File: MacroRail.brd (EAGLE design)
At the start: 42.9 x 81.5 mm, 20 parts, among them CN1 1X4-3.5MM, J1 SJ1-2503A, U1 ESP32DEVKITC, U2 TCM2209-V1.2

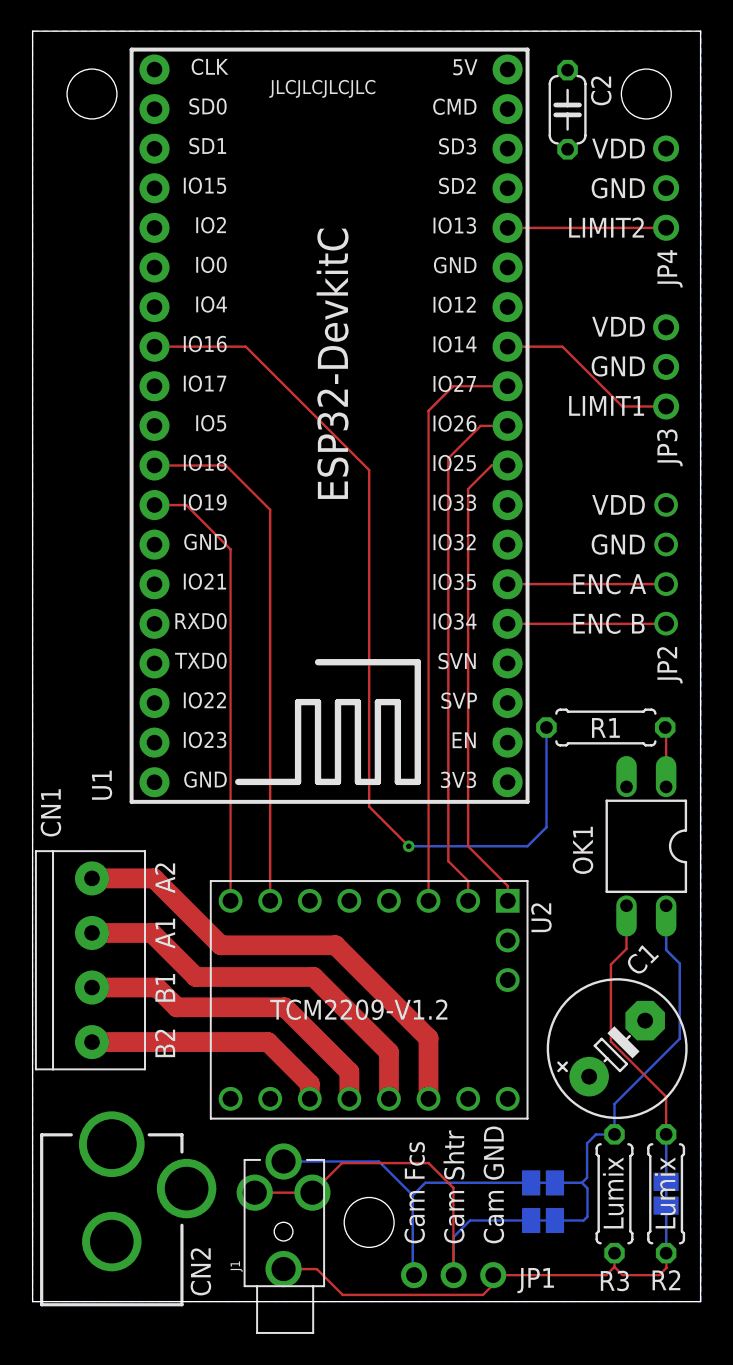
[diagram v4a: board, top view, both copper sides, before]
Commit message: Start V1.1 design
Add UART Communication between TCM and ESP via SD2 and SD3 pins. Connect DIAG pin. Still undecided whether INDEX pin is necessary as this pin is not always easily accessible on TCM boards.
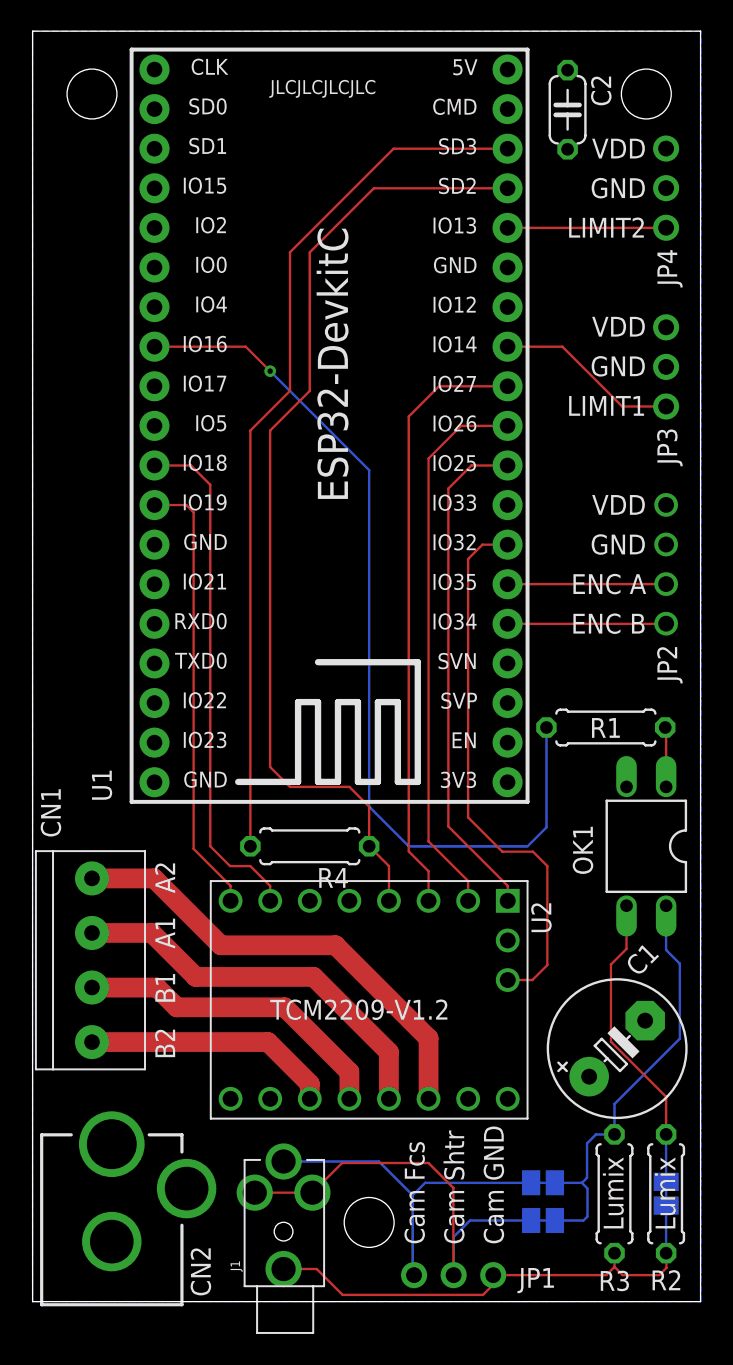
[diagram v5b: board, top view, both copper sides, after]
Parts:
- added R4: 1k, rcl:0207/7
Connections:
- removed net STEP_PDN_1: U2.PDN_1
- removed net STEP_UART_CLK: U2.CLK
- new net N$2: U1.8
- new net STEP_DIAG: U1.7, U2.DIAG
- new net U1RXD: R4.1, U1.16, U2.PDN_1
- new net U1TXD: R4.2, U1.17
- net GND: now also U2.CLK
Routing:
- net U1RXD: track 0.00 -> 62.4 mm
- net U1TXD: track 0.00 -> 55.9 mm
- net STEP_DIAG: track 0.00 -> 35.2 mm
- net STEP_EN: track 30.6 -> 32.4 mm
- net STEP_MS1: track 33.6 -> 35.4 mm
- net STEP_MS2: track 37.2 -> 38.7 mm
- net STEP: track 33.7 -> 33.1 mm
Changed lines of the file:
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@@
 <attribute name="VALUE" x="31.526" y="78.746" size="1.27" layer="27" ratio="10" rot="R270"/>
+</element>
+<element name="R4" library="rcl" library_urn="urn:adsk.eagle:library:334" package="0207/7" package3d_urn="urn:adsk.eagle:package:23493/2" value="1k" x="17.78" y="29.21" smashed="yes" rot="R180">
+<attribute name="NAME" x="20.32" y="27.813" size="1.27" layer="25" ratio="10" rot="R180"/>
+<attribute name="POPULARITY" value="22" x="17.78" y="29.21" size="1.778" layer="27" rot="R180" display="off"/>
+<attribute name="SPICEPREFIX" value="R" x="17.78" y="29.21" size="1.778" layer="27" rot="R180" display="off"/>
+<attribute name="VALUE" x="20.066" y="29.7688" size="1.27" layer="27" ratio="10" rot="R180"/>
 </element>
 </elements>
@@
 <contactref element="OK1" pad="2"/>
 <contactref element="C2" pad="1"/>
+<contactref element="U2" pad="CLK"/>
 </signal>
 <signal name="A2" class="1">
@@
 <contactref element="U2" pad="EN"/>
 <contactref element="U1" pad="9"/>
-<wire x1="30.47" y1="53.64" x2="29.454" y2="53.64" width="0.1524" layer="1"/>
-<wire x1="29.454" y1="53.64" x2="27.94" y2="52.126" width="0.1524" layer="1"/>
-<wire x1="27.94" y1="29.21" x2="30.48" y2="26.67" width="0.1524" layer="1"/>
+<wire x1="30.47" y1="53.64" x2="28.154" y2="53.64" width="0.1524" layer="1"/>
+<wire x1="28.154" y1="53.64" x2="26.67" y2="52.156" width="0.1524" layer="1"/>
+<wire x1="26.67" y1="30.48" x2="30.48" y2="26.67" width="0.1524" layer="1"/>
 <wire x1="30.48" y1="26.67" x2="30.48" y2="25.71" width="0.1524" layer="1"/>
-<wire x1="27.94" y1="52.126" x2="27.94" y2="29.21" width="0.1524" layer="1"/>
+<wire x1="26.67" y1="52.156" x2="26.67" y2="30.48" width="0.1524" layer="1"/>
 </signal>
 <signal name="STEP_MS1">
 <contactref element="U2" pad="MS1"/>
 <contactref element="U1" pad="10"/>
-<wire x1="26.67" y1="54.102" x2="26.67" y2="28.25" width="0.1524" layer="1"/>
+<wire x1="25.4" y1="54.092" x2="25.4" y2="29.52" width="0.1524" layer="1"/>
 <wire x1="27.94" y1="25.71" x2="27.94" y2="26.98" width="0.1524" layer="1"/>
-<wire x1="27.94" y1="26.98" x2="26.67" y2="28.25" width="0.1524" layer="1"/>
-<wire x1="28.748" y1="56.18" x2="30.47" y2="56.18" width="0.1524" layer="1"/>
-<wire x1="26.67" y1="54.102" x2="28.748" y2="56.18" width="0.1524" layer="1"/>
+<wire x1="27.94" y1="26.98" x2="25.4" y2="29.52" width="0.1524" layer="1"/>
+<wire x1="27.488" y1="56.18" x2="30.47" y2="56.18" width="0.1524" layer="1"/>
+<wire x1="25.4" y1="54.092" x2="27.488" y2="56.18" width="0.1524" layer="1"/>
 </signal>
 <signal name="STEP_MS2">
 <contactref element="U2" pad="MS2"/>
 <contactref element="U1" pad="11"/>
-<wire x1="25.4" y1="25.71" x2="25.4" y2="57.15" width="0.1524" layer="1"/>
-<wire x1="26.97" y1="58.72" x2="30.47" y2="58.72" width="0.1524" layer="1"/>
-<wire x1="25.4" y1="57.15" x2="26.97" y2="58.72" width="0.1524" layer="1"/>
-</signal>
-<signal name="STEP_PDN_1">
-<contactref element="U2" pad="PDN_1"/>
+<wire x1="24.13" y1="56.78" x2="24.13" y2="28.88" width="0.1524" layer="1"/>
+<wire x1="25.4" y1="25.71" x2="25.4" y2="27.61" width="0.1524" layer="1"/>
+<wire x1="25.4" y1="27.61" x2="24.13" y2="28.88" width="0.1524" layer="1"/>
+<wire x1="26.07" y1="58.72" x2="30.47" y2="58.72" width="0.1524" layer="1"/>
+<wire x1="24.13" y1="56.78" x2="26.07" y2="58.72" width="0.1524" layer="1"/>
 </signal>
 <signal name="STEP_PDN_2">
 <contactref element="U2" pad="PDN_2"/>
-</signal>
-<signal name="STEP_UART_CLK">
-<contactref element="U2" pad="CLK"/>
 </signal>
 <signal name="STEP">
 <contactref element="U2" pad="STEP"/>
 <contactref element="U1" pad="30"/>
-<wire x1="15.24" y1="25.71" x2="15.24" y2="50.8" width="0.1524" layer="1"/>
-<wire x1="12.4" y1="53.64" x2="7.82" y2="53.64" width="0.1524" layer="1"/>
-<wire x1="15.24" y1="50.8" x2="12.4" y2="53.64" width="0.1524" layer="1"/>
+<wire x1="15.24" y1="25.71" x2="15.24" y2="26.67" width="0.1524" layer="1"/>
+<wire x1="15.24" y1="26.67" x2="13.97" y2="27.94" width="0.1524" layer="1"/>
+<wire x1="7.82" y1="53.64" x2="10.16" y2="53.64" width="0.1524" layer="1"/>
+<wire x1="10.16" y1="53.64" x2="11.4" y2="52.4" width="0.1524" layer="1"/>
+<wire x1="11.4" y1="29.21" x2="11.4" y2="52.4" width="0.1524" layer="1"/>
+<wire x1="12.67" y1="27.94" x2="11.4" y2="29.21" width="0.1524" layer="1"/>
+<wire x1="13.97" y1="27.94" x2="12.67" y2="27.94" width="0.1524" layer="1"/>
 </signal>
 <signal name="STEP_DIR">
@@
 <contactref element="U1" pad="31"/>
 <wire x1="9.86" y1="51.1" x2="7.82" y2="51.1" width="0.1524" layer="1"/>
-<wire x1="12.7" y1="25.71" x2="12.7" y2="48.26" width="0.1524" layer="1"/>
-<wire x1="12.7" y1="48.26" x2="9.86" y2="51.1" width="0.1524" layer="1"/>
+<wire x1="12.7" y1="25.71" x2="12.7" y2="26.67" width="0.1524" layer="1"/>
+<wire x1="10.33" y1="50.63" x2="9.86" y2="51.1" width="0.1524" layer="1"/>
+<wire x1="12.7" y1="26.67" x2="10.33" y2="29.04" width="0.1524" layer="1"/>
+<wire x1="10.33" y1="29.04" x2="10.33" y2="50.63" width="0.1524" layer="1"/>
 </signal>
 <signal name="SHUTTER">
@@
 <contactref element="R1" pad="2"/>
 <wire x1="7.82" y1="61.26" x2="13.67" y2="61.26" width="0.1524" layer="1"/>
-<wire x1="21.59" y1="31.75" x2="24.13" y2="29.21" width="0.1524" layer="1"/>
-<via x="24.13" y="29.21" extent="1-16" drill="0.35"/>
-<wire x1="13.67" y1="61.26" x2="21.59" y2="53.34" width="0.1524" layer="1"/>
-<wire x1="21.59" y1="53.34" x2="21.59" y2="31.75" width="0.1524" layer="1"/>
+<wire x1="13.67" y1="61.26" x2="15.24" y2="59.69" width="0.1524" layer="1"/>
 <wire x1="24.13" y1="29.21" x2="31.75" y2="29.21" width="0.1524" layer="16"/>
 <wire x1="32.964" y1="36.83" x2="32.964" y2="30.424" width="0.1524" layer="16"/>
 <wire x1="32.964" y1="30.424" x2="31.75" y2="29.21" width="0.1524" layer="16"/>
+<wire x1="24.13" y1="29.21" x2="21.59" y2="31.75" width="0.1524" layer="16"/>
+<wire x1="21.59" y1="53.34" x2="15.24" y2="59.69" width="0.1524" layer="16"/>
+<via x="15.24" y="59.69" extent="1-16" drill="0.35"/>
+<wire x1="21.59" y1="31.75" x2="21.59" y2="53.34" width="0.1524" layer="16"/>
 </signal>
 <signal name="LIMIT1">
@@
 <wire x1="40.64" y1="36.774" x2="40.64" y2="33.02" width="0.1524" layer="1"/>
 </signal>
+<signal name="U1TXD">
+<contactref element="R4" pad="2"/>
+<contactref element="U1" pad="17"/>
+<wire x1="30.47" y1="73.96" x2="23.16" y2="73.96" width="0.1524" layer="1"/>
+<wire x1="16.51" y1="67.31" x2="16.51" y2="58.42" width="0.1524" layer="1"/>
+<wire x1="16.51" y1="58.42" x2="13.97" y2="55.88" width="0.1524" layer="1"/>
+<wire x1="13.97" y1="55.88" x2="13.97" y2="29.21" width="0.1524" layer="1"/>
+<wire x1="23.16" y1="73.96" x2="16.51" y2="67.31" width="0.1524" layer="1"/>
+</signal>
+<signal name="U1RXD">
+<contactref element="R4" pad="1"/>
+<contactref element="U2" pad="PDN_1"/>
+<contactref element="U1" pad="16"/>
+<wire x1="21.59" y1="29.21" x2="21.59" y2="31.75" width="0.1524" layer="1"/>
+<wire x1="21.59" y1="31.75" x2="20.32" y2="33.02" width="0.1524" layer="1"/>
+<wire x1="20.32" y1="33.02" x2="16.51" y2="33.02" width="0.1524" layer="1"/>
+<wire x1="16.51" y1="33.02" x2="15.24" y2="34.29" width="0.1524" layer="1"/>
+<wire x1="15.24" y1="55.88" x2="17.78" y2="58.42" width="0.1524" layer="1"/>
+<wire x1="17.78" y1="58.42" x2="17.78" y2="67.31" width="0.1524" layer="1"/>
+<wire x1="17.78" y1="67.31" x2="21.89" y2="71.42" width="0.1524" layer="1"/>
+<wire x1="21.89" y1="71.42" x2="30.47" y2="71.42" width="0.1524" layer="1"/>
+<wire x1="15.24" y1="34.29" x2="15.24" y2="55.88" width="0.1524" layer="1"/>
+<wire x1="22.86" y1="25.71" x2="22.86" y2="27.94" width="0.1524" layer="1"/>
+<wire x1="22.86" y1="27.94" x2="21.59" y2="29.21" width="0.1524" layer="1"/>
+</signal>
+<signal name="STEP_DIAG">
+<contactref element="U2" pad="DIAG"/>
+<contactref element="U1" pad="7"/>
+<wire x1="30.47" y1="48.56" x2="28.86" y2="48.56" width="0.1524" layer="1"/>
+<wire x1="28.86" y1="48.56" x2="27.94" y2="47.64" width="0.1524" layer="1"/>
+<wire x1="27.94" y1="47.64" x2="27.94" y2="31.06" width="0.1524" layer="1"/>
+<wire x1="33.02" y1="21.59" x2="32.06" y2="20.63" width="0.1524" layer="1"/>
+<wire x1="32.06" y1="20.63" x2="30.48" y2="20.63" width="0.1524" layer="1"/>
+<wire x1="27.94" y1="31.06" x2="30.135" y2="28.865" width="0.1524" layer="1"/>
+<wire x1="30.135" y1="28.865" x2="32.095" y2="28.865" width="0.1524" layer="1"/>
+<wire x1="32.095" y1="28.865" x2="33.02" y2="27.94" width="0.1524" layer="1"/>
+<wire x1="33.02" y1="27.94" x2="33.02" y2="21.59" width="0.1524" layer="1"/>
+</signal>
+<signal name="N$2">
+<contactref element="U1" pad="8"/>
+</signal>
 </signals>

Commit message: Connect DIAG
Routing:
- net U1TXD: track 55.9 -> 58.1 mm
- net U1RXD: track 62.4 -> 63.2 mm
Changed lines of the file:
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@@
 <contactref element="R4" pad="2"/>
 <contactref element="U1" pad="17"/>
-<wire x1="30.47" y1="73.96" x2="23.16" y2="73.96" width="0.1524" layer="1"/>
-<wire x1="16.51" y1="67.31" x2="16.51" y2="58.42" width="0.1524" layer="1"/>
+<wire x1="30.47" y1="73.96" x2="19.35" y2="73.96" width="0.1524" layer="1"/>
+<wire x1="16.51" y1="71.12" x2="16.51" y2="58.42" width="0.1524" layer="1"/>
 <wire x1="16.51" y1="58.42" x2="13.97" y2="55.88" width="0.1524" layer="1"/>
 <wire x1="13.97" y1="55.88" x2="13.97" y2="29.21" width="0.1524" layer="1"/>
-<wire x1="23.16" y1="73.96" x2="16.51" y2="67.31" width="0.1524" layer="1"/>
+<wire x1="19.35" y1="73.96" x2="16.51" y2="71.12" width="0.1524" layer="1"/>
 </signal>
 <signal name="U1RXD">
@@
 <wire x1="20.32" y1="33.02" x2="16.51" y2="33.02" width="0.1524" layer="1"/>
 <wire x1="16.51" y1="33.02" x2="15.24" y2="34.29" width="0.1524" layer="1"/>
-<wire x1="15.24" y1="55.88" x2="17.78" y2="58.42" width="0.1524" layer="1"/>
-<wire x1="17.78" y1="58.42" x2="17.78" y2="67.31" width="0.1524" layer="1"/>
-<wire x1="17.78" y1="67.31" x2="21.89" y2="71.42" width="0.1524" layer="1"/>
-<wire x1="21.89" y1="71.42" x2="30.47" y2="71.42" width="0.1524" layer="1"/>
-<wire x1="15.24" y1="34.29" x2="15.24" y2="55.88" width="0.1524" layer="1"/>
+<wire x1="15.24" y1="54.61" x2="17.78" y2="57.15" width="0.1524" layer="1"/>
+<wire x1="17.78" y1="57.15" x2="17.78" y2="68.58" width="0.1524" layer="1"/>
+<wire x1="17.78" y1="68.58" x2="20.62" y2="71.42" width="0.1524" layer="1"/>
+<wire x1="20.62" y1="71.42" x2="30.47" y2="71.42" width="0.1524" layer="1"/>
+<wire x1="15.24" y1="34.29" x2="15.24" y2="54.61" width="0.1524" layer="1"/>
 <wire x1="22.86" y1="25.71" x2="22.86" y2="27.94" width="0.1524" layer="1"/>
 <wire x1="22.86" y1="27.94" x2="21.59" y2="29.21" width="0.1524" layer="1"/>

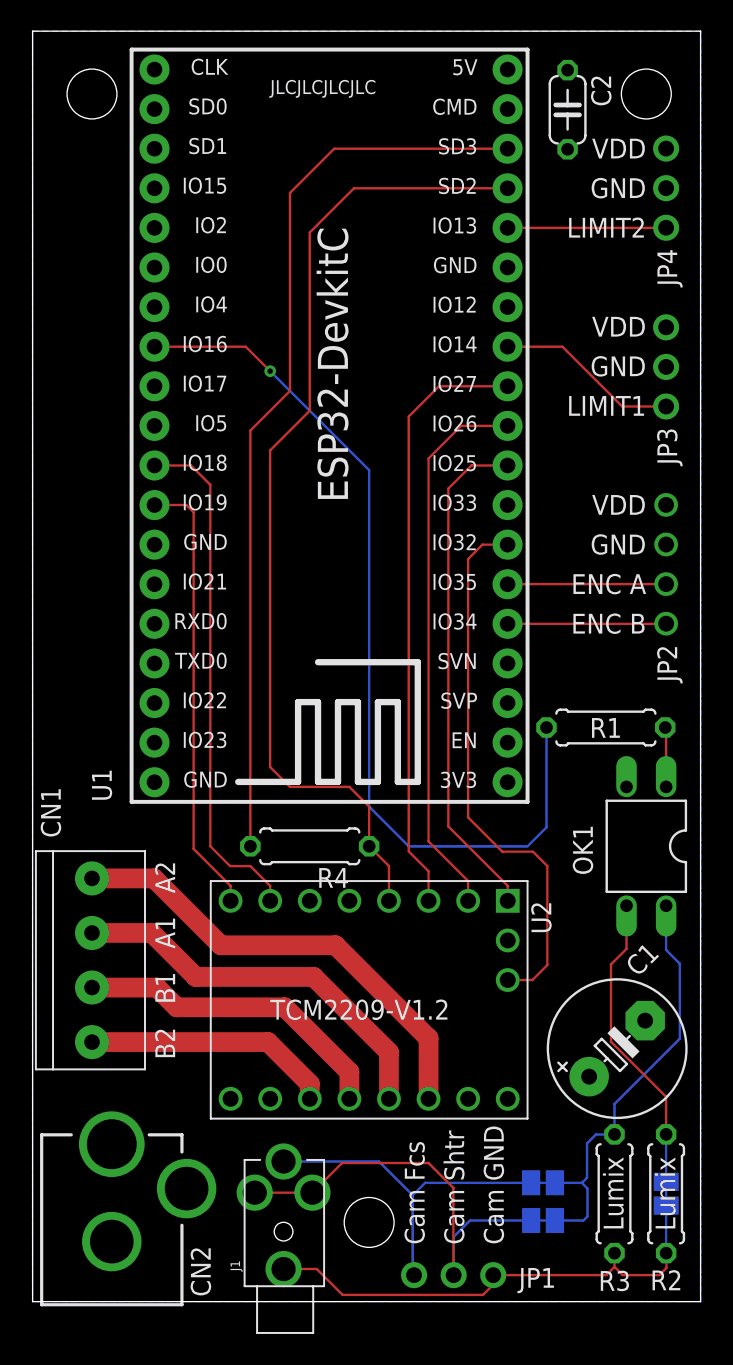
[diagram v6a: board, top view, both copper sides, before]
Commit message: V1.1
Add optional index pin and produce new output files
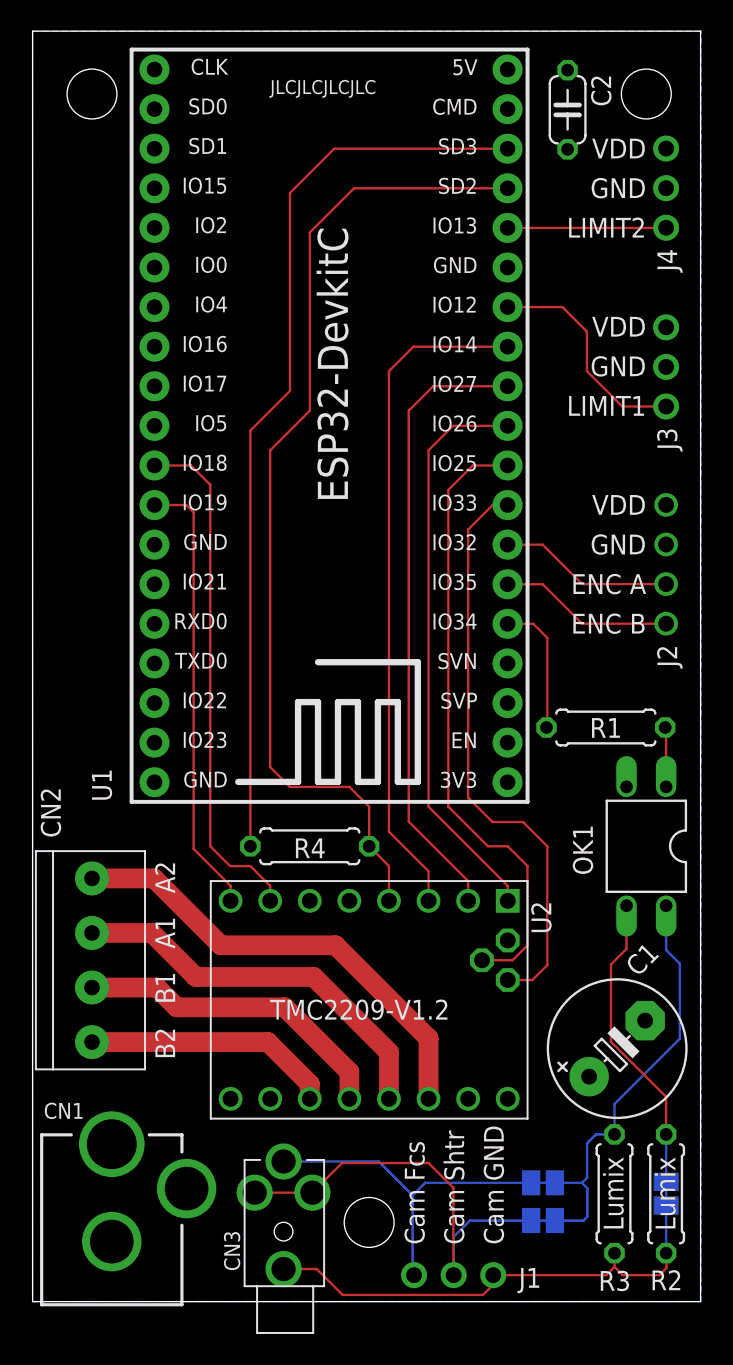
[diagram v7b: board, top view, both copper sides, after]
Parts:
- removed JP1: (no value), adafruit:1X03-CLEANBIG
- added CN3: SJ1-2503A, 00-Random-Components-Simen:STEREOJACK2.5MM_STEREOJACK2.5MM
- CN1: value 1X4-3.5MM -> (none); device adafruit:1X04-3.5MM -> adafruit:DCJACK_2MM_PTH
- CN2: value (none) -> 1X4-3.5MM; device adafruit:DCJACK_2MM_PTH -> adafruit:1X04-3.5MM
- J1: value SJ1-2503A -> (none); device 00-Random-Components-Simen:STEREOJACK2.5MM_STEREOJACK2.5MM -> adafruit:1X03-CLEANBIG
- U2: value TCM2209-V1.2 -> TMC2209-V1.2+INDEX; device 00-Random-Components-Simen:BIGTREETECH-TCM2209-V1.2 -> 00-Random-Components-Simen:BIGTREETECH-TMC2209-V1.2+INDEX
- moved CN1 25.4 mm to (5.08, -3.50), turned to 0 degrees
- moved CN2 25.4 mm to (3.81, 21.9), turned to 270 degrees
- moved J1 11.3 mm to (27.0, 1.70), turned to 0 degrees
- renumbered JP2 to J2, JP3 to J3, JP4 to J4
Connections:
- removed net N$2: U1.8
- new net STEP_CLK: U2.CLK
- new net STEP_INDEX: U1.9, U2.INDEX
- net A1: now also CN2.2; no longer CN1.2
- net A2: now also CN2.1; no longer CN1.1
- net B1: now also CN2.3; no longer CN1.3
- net B2: now also CN2.4; no longer CN1.4
- net CAM_FOCUS_SHUTTER: now also CN3.RING, CN3.TIP1, CN3.TIP2, J1.1, J1.2; no longer J1.RING, J1.TIP1, J1.TIP2, JP1.1, JP1.2
- net CAM_GND: now also CN3.SHIELD, J1.3; no longer J1.SHIELD, JP1.3
- net ENC_A: now also U1.7; no longer U1.6
- net ENC_B: now also U1.6; no longer U1.5
- net GND: now also CN1.GND, CN1.GNDBREAK; no longer CN2.GND, CN2.GNDBREAK, U2.CLK
- net LIMIT1: now also U1.13; no longer U1.12
- net SHUTTER: now also U1.5; no longer U1.27
- net STEP_DIAG: now also U1.8; no longer U1.7
- net STEP_EN: now also U1.10; no longer U1.9
- net STEP_MS1: now also U1.11; no longer U1.10
- net STEP_MS2: now also U1.12; no longer U1.11
- net V_MOTOR: now also CN1.PWR; no longer CN2.PWR
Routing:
- net SHUTTER: track 58.0 -> 8.70 mm, vias 1 -> 0
- net STEP_INDEX: track 0.00 -> 39.8 mm
- net STEP_MS1: track 35.4 -> 40.0 mm
- net STEP_MS2: track 38.7 -> 43.3 mm
- net STEP_EN: track 32.4 -> 36.7 mm
- net LIMIT1: track 11.8 -> 14.3 mm
- net STEP_DIAG: track 35.2 -> 37.3 mm
- net ENC_A: track 10.2 -> 11.2 mm
- net ENC_B: track 10.2 -> 11.2 mm
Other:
- board text added: "Index-pin not always present on TMC2209"
- board text added: "Mar 2022"
- board text added: "Motorized Macro Slider V1.1"
- board text added: "TMC2209-V1.2"
- board text removed: "Feb 2022"
- board text removed: "Motorized Macro Slider V1.0"
- board text removed: "TCM2209-V1.2"
